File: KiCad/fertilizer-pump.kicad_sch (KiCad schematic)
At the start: 4 parts, among them U2 ESP32-S3-WROOM-1

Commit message: Save project baseline before power supply and USB changes
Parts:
- added J1: Conn_01x04, symbol Connector_Generic:Conn_01x04
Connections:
- net +3.3V: now also A1.10 (VDD), A2.10 (VDD); no longer A1.15 (GND), A2.15 (GND)
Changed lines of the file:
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@@
 		(pin "14"
 		)
-		(pin "15"
+		(pin "10"
 		)
 		(instances
@@
 	)
 	(symbol
-		(lib_name "BTT TMC2209_1")
 		(lib_id "fertilizer-pump:BTT TMC2209")
 		(at 128.27 62.23 0)
@@
 		(pin "14"
 		)
-		(pin "15"
+		(pin "10"
 		)
 		(instances
@@
 					(unit 1)
 				)
+			)
+		)
+	)
+	(symbol
+		(lib_id "Connector_Generic:Conn_01x04")
+		(at 72.39 111.76 0)
+		(unit 1)
+		(body_style 1)
+		(exclude_from_sim no)
+		(in_bom yes)
+		(on_board yes)
+		(in_pos_files yes)
+		(dnp no)
+		(fields_autoplaced yes)
+		(property "Reference" "J1"
+			(at 74.93 111.7599 0)
+			(show_name no)
+			(do_not_autoplace no)
+			(effects
+				(font
+					(size 1.27 1.27)
+				)
+				(justify left)
+			)
+		)
+		(property "Value" "Conn_01x04"
+			(at 74.93 114.2999 0)
+			(show_name no)
+			(do_not_autoplace no)
+			(effects
+				(font
+					(size 1.27 1.27)
+				)
+				(justify left)
+			)
+		)
+		(property "Footprint" ""
+			(at 72.39 111.76 0)
+			(hide yes)
+			(show_name no)
+			(do_not_autoplace no)
+			(effects
+				(font
+					(size 1.27 1.27)
+				)
+			)
+		)
+		(property "Datasheet" ""
+			(at 72.39 111.76 0)
+			(hide yes)
+			(show_name no)
+			(do_not_autoplace no)
+			(effects
+				(font
+					(size 1.27 1.27)
+				)
+			)
+		)
+		(property "Description" "Generic connector, single row, 01x04, script generated (kicad-library-utils/schlib/autogen/connector/)"
+			(at 72.39 111.76 0)
+			(hide yes)
+			(show_name no)
+			(do_not_autoplace no)
+			(effects
+				(font
+					(size 1.27 1.27)
+				)
+			)
+		)
+		(pin "1"
+		)
+		(pin "3"
+		)
+		(pin "4"
+		)
+		(pin "2"
+		)
+		(instances
+			(project "fertilizer-pump"
+				(path "/156e031f-7691-48a3-975c-ba45ae33e444"
+					(reference "J1")
+					(unit 1)
+				)

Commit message: add motor connector
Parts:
- added J2: Conn_01x04, Connector_JST:JST_XH_B4B-XH-A_1x04_P2.50mm_Vertical, symbol Connector_Generic:Conn_01x04
- added R2, R3: 10K, symbol Device:R_Small
- J1: footprint (none) -> Connector_JST:JST_XH_B4B-XH-A_1x04_P2.50mm_Vertical
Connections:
- net +3.3V: now also R2.2, R3.2
- net DRIV1.A1: now also J1.4 (Pin_4)
- net DRIV1.A2: now also J1.2 (Pin_2)
- net DRIV1.B1: now also J1.3 (Pin_3)
- net DRIV1.B2: now also J1.1 (Pin_1)
- net DRIV1.DIR: now also U2.6 (GPIO6/TOUCH6/ADC1_CH5)
- net DRIV1.STEP: now also U2.5 (GPIO5/TOUCH5/ADC1_CH4)
- net DRIV2.A1: now also J2.4 (Pin_4)
- net DRIV2.A2: now also J2.2 (Pin_2)
- net DRIV2.B1: now also J2.3 (Pin_3)
- net DRIV2.B2: now also J2.1 (Pin_1)
- net DRIV2.DIR: now also U2.17 (GPIO9/TOUCH9/ADC1_CH8/FSPIHD/SUBSPIHD)
- net DRIV2.STEP: now also U2.12 (GPIO8/TOUCH8/ADC1_CH7/SUBSPICS1)
- net DRIV.ENABLE: now reaches A1.1 (ENABLE)
- net DRIV.ENABLE: now also A2.1 (ENABLE)
- net DRIV.UART.RX_{uC}: now reaches U2.38 (GPIO2/TOUCH2/ADC1_CH1)
- net DRIV.UART.TX_{MCU}: now reaches U2.39 (GPIO1/TOUCH1/ADC1_CH0)
- net ~{DRIV1.ENABLE}: now reaches U2.4 (GPIO4/TOUCH4/ADC1_CH3)
- net ~{DRIV2.ENABLE}: now reaches U2.7 (GPIO7/TOUCH7/ADC1_CH6)
- new net DRIV1.ENABLE: R3.1
- new net DRIV2.ENABLE: R2.1
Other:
- moved on the sheet: J1

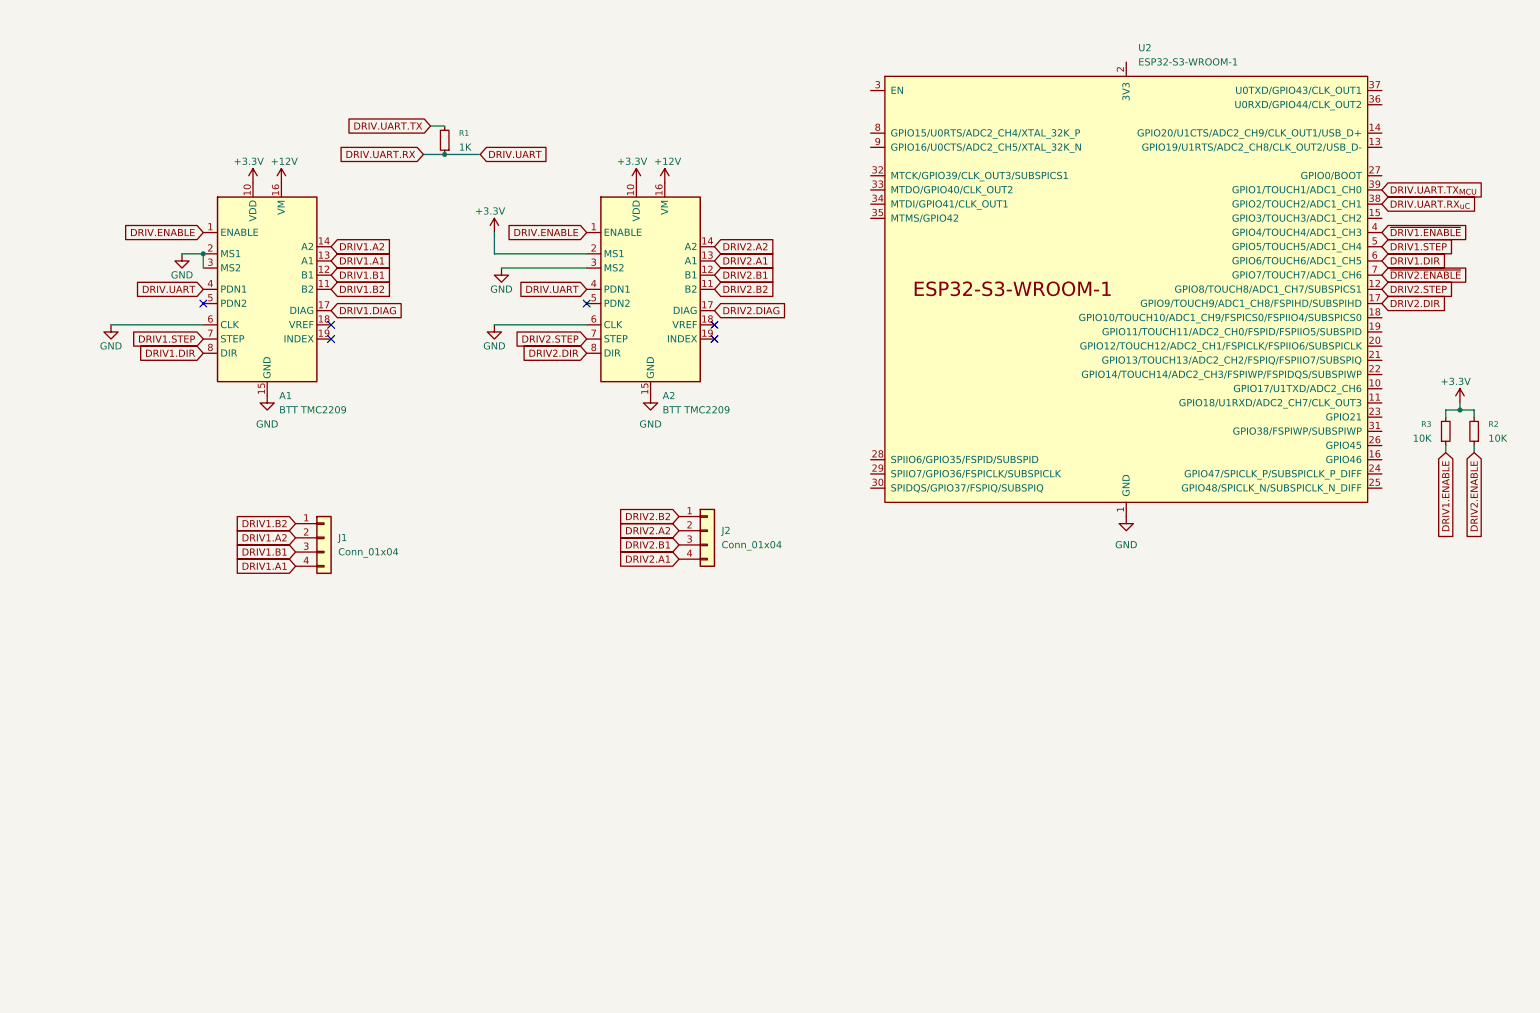
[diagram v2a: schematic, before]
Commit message: add pd trigger board, usb-c
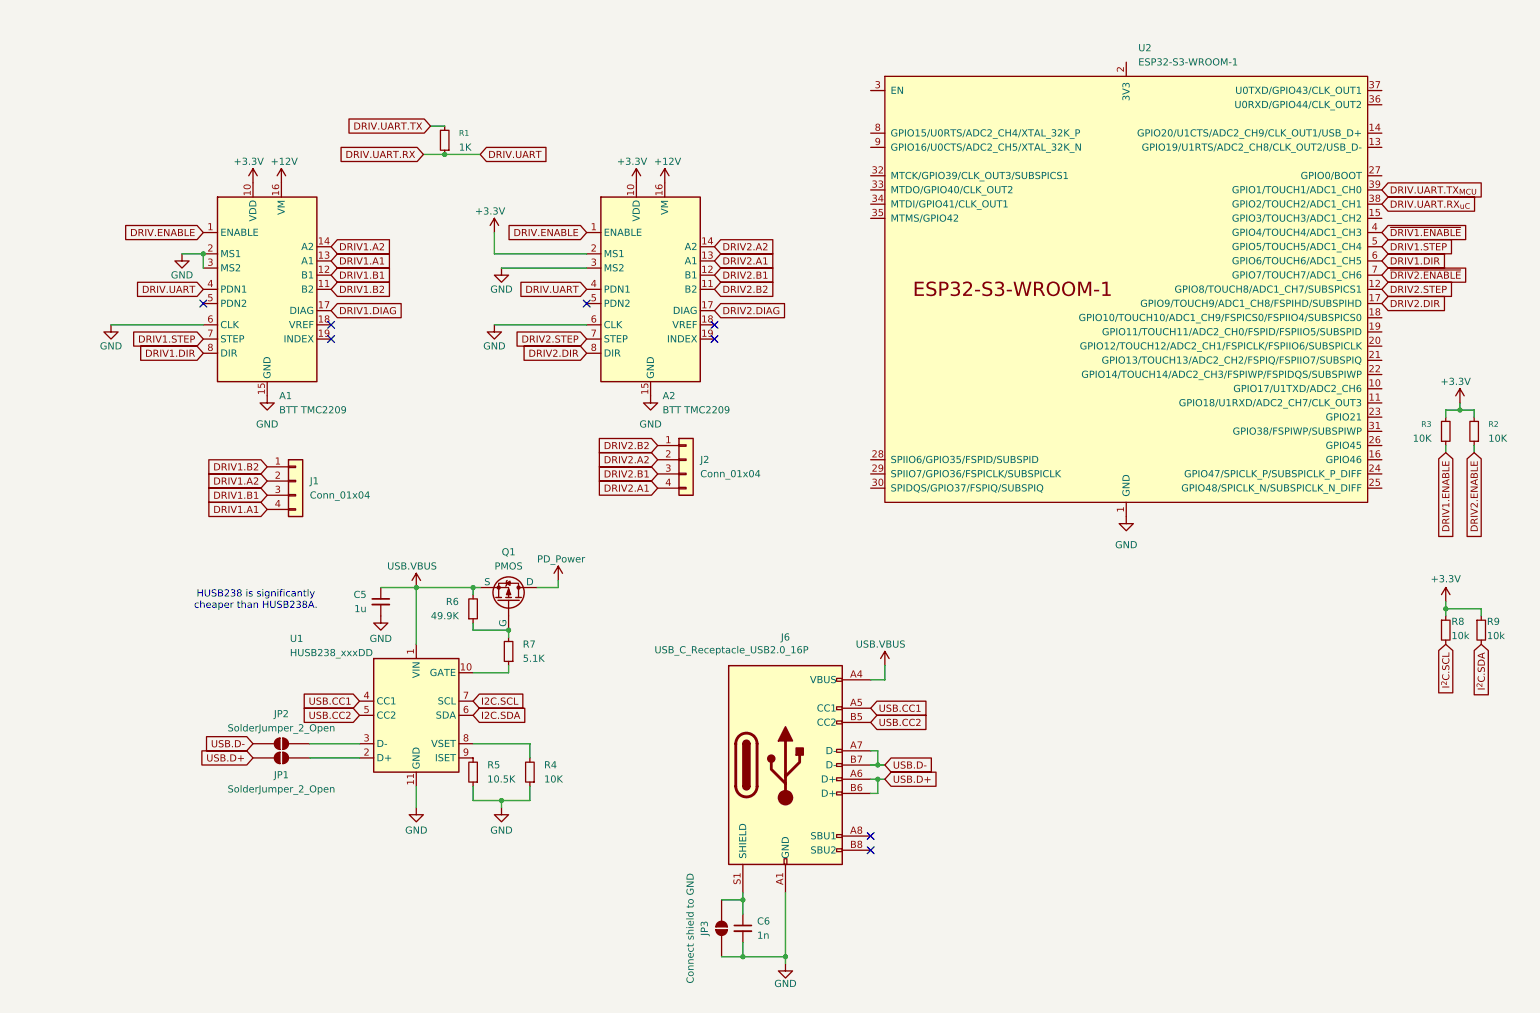
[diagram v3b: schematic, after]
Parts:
- added C5: 1u, Capacitor_SMD:C_0805_2012Metric_Pad1.18x1.45mm_HandSolder, symbol Device:C_Small
- added C6: 1n, Capacitor_SMD:C_0805_2012Metric_Pad1.18x1.45mm_HandSolder, symbol Device:C_Small
- added J6: USB_C_Receptacle_USB2.0_16P, Connector_USB:USB_C_Receptacle_GCT_USB4105-xx-A_16P_TopMnt_Horizontal, symbol Connector:USB_C_Receptacle_USB2.0_16P
- added JP1, JP2: SolderJumper_2_Open, symbol Jumper:SolderJumper_2_Open
- added JP3: Connect shield to GND, symbol Jumper:SolderJumper_2_Open
- added Q1: PMOS, symbol Simulation_SPICE:PMOS
- added R4: 10K, symbol Device:R_Small
- added R5: 10.5K, symbol Device:R_Small
- added R6: 49.9K, symbol Device:R_Small
- added R7: 5.1K, symbol Device:R_Small
- added R8, R9: 10k, Resistor_SMD:R_0805_2012Metric_Pad1.20x1.40mm_HandSolder, symbol Device:R_Small
- added U1: HUSB238_xxxDD, Package_DFN_QFN:WDFN-10-1EP_3x3mm_P0.5mm_EP1.8x2.5mm_ThermalVias, symbol Interface_USB:HUSB238_xxxDD
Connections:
- net +3.3V: now also R8.1, R9.1
- net GND: now also C5.2, C6.2, J6.A1 (GND), J6.A12 (GND), J6.B1 (GND), J6.B12 (GND), JP3.1 (A), R4.1, R5.1, U1.11 (GND)
- new net: Q1.2 (G), R6.1, R7.2
- new net: JP1.2 (B), U1.2 (D+)
- new net: C6.1, J6.S1 (SHIELD), JP3.2 (B)
- new net: R4.2, U1.8 (VSET)
- new net: R5.2, U1.9 (ISET)
- new net: JP2.2 (B), U1.3 (D-)
- new net: R7.1, U1.10 (GATE)
- new net I2C.SCL: U1.7 (SCL)
- new net I2C.SDA: U1.6 (SDA)
- new net I^{2}C.SCL: R8.2
- new net I^{2}C.SDA: R9.2
- new net PD_Power: Q1.1 (D)
- new net USB.CC1: J6.A5 (CC1), U1.4 (CC1)
- new net USB.CC2: J6.B5 (CC2), U1.5 (CC2)
- new net USB.D+: J6.A6 (D+), J6.B6 (D+), JP1.1 (A)
- new net USB.D-: J6.A7 (D-), J6.B7 (D-), JP2.1 (A)
- new net USB.VBUS: C5.1, J6.A4 (VBUS), J6.A9 (VBUS), J6.B4 (VBUS), J6.B9 (VBUS), Q1.3 (S), R6.2, U1.1 (VIN)
- no-connect marks 6 -> 8
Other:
- note added: "HUSB238 is significantly cheaper than HUSB238A."
- moved on the sheet: J1, J2

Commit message: .
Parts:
- added D1, D2: ESD762, Package_TO_SOT_SMD:SOT-23_Handsoldering, symbol Device:D_TVS_Dual_AAC
- added D3: D_Zener, Diode_SMD:D_SOD-123F, symbol Device:D_Zener
- A1, A2: footprint Module:Pololu_Breakout-16_15.2x20.3mm -> fertilizer-pump:BTT TMC2209
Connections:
- net GND: now also D1.3 (common), D2.3 (common), D3.2 (A)
- net USB.CC1: now also D2.1 (A1)
- net USB.CC2: now also D2.2 (A2)
- net USB.D+: now also D1.1 (A1)
- net USB.D-: now also D1.2 (A2)
- net USB.VBUS: now also D3.1 (K)
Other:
- note added: "ESD Protection"
- note added: "FIX: wrong footprint SOD123FL instead of SOD123F"
- moved on the sheet: C5, JP1, JP2, Q1, R4, R5, R6, R7, U1

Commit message: refactor,
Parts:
- removed A1, A2: BTT TMC2209, fertilizer-pump:BTT TMC2209, symbol fertilizer-pump:BTT TMC2209
- removed C5: 1u, Capacitor_SMD:C_0805_2012Metric_Pad1.18x1.45mm_HandSolder, symbol Device:C_Small
- removed C6: 1n, Capacitor_SMD:C_0805_2012Metric_Pad1.18x1.45mm_HandSolder, symbol Device:C_Small
- removed D1, D2: ESD762, Package_TO_SOT_SMD:SOT-23_Handsoldering, symbol Device:D_TVS_Dual_AAC
- removed D3: D_Zener, Diode_SMD:D_SOD-123F, symbol Device:D_Zener
- removed J1, J2: Conn_01x04, Connector_JST:JST_XH_B4B-XH-A_1x04_P2.50mm_Vertical, symbol Connector_Generic:Conn_01x04
- removed J6: USB_C_Receptacle_USB2.0_16P, Connector_USB:USB_C_Receptacle_GCT_USB4105-xx-A_16P_TopMnt_Horizontal, symbol Connector:USB_C_Receptacle_USB2.0_16P
- removed JP1, JP2: SolderJumper_2_Open, symbol Jumper:SolderJumper_2_Open
- removed JP3: Connect shield to GND, symbol Jumper:SolderJumper_2_Open
- removed Q1: PMOS, symbol Simulation_SPICE:PMOS
- removed R1: 1K, symbol Device:R_Small
- removed R4: 10K, symbol Device:R_Small
- removed R5: 10.5K, symbol Device:R_Small
- removed R6: 49.9K, symbol Device:R_Small
- removed R7: 5.1K, symbol Device:R_Small
- removed U1: HUSB238_xxxDD, Package_DFN_QFN:WDFN-10-1EP_3x3mm_P0.5mm_EP1.8x2.5mm_ThermalVias, symbol Interface_USB:HUSB238_xxxDD
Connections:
- no-connect marks 8 -> 0
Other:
- added sheet Power (power.kicad_sch)
- added sheet Stepper (stepper.kicad_sch)
- note removed: "ESD Protection"
- note removed: "FIX: wrong footprint SOD123FL instead of SOD123F"
- note removed: "HUSB238 is significantly cheaper than HUSB238A."

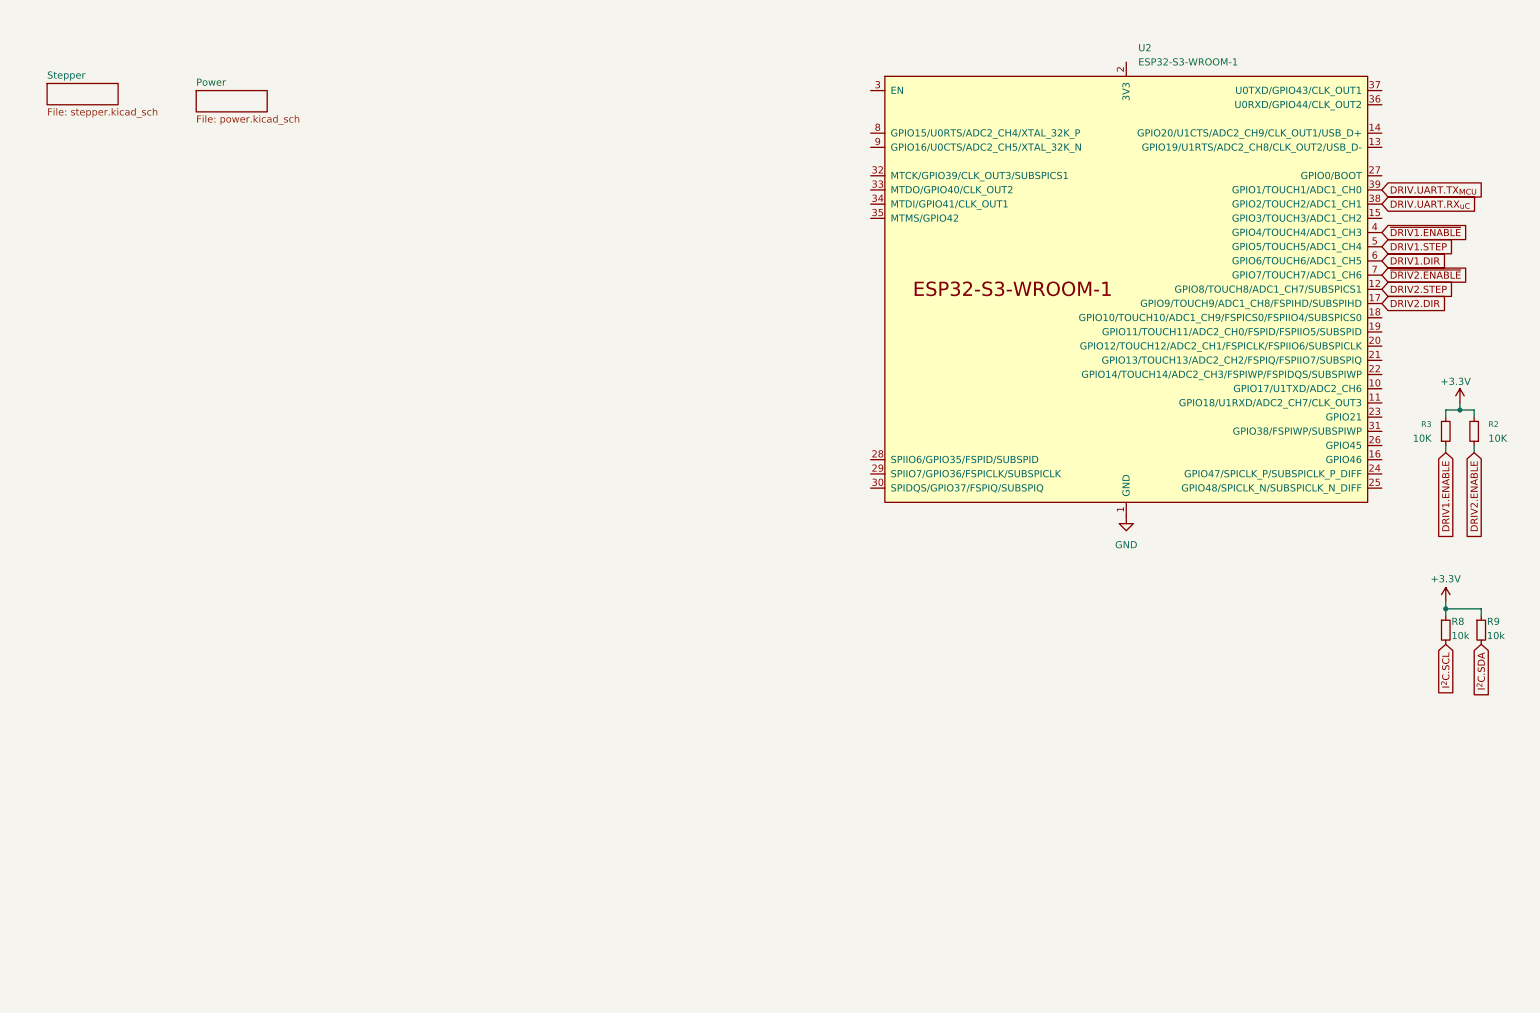
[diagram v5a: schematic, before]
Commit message: add buck converter, fix footprints
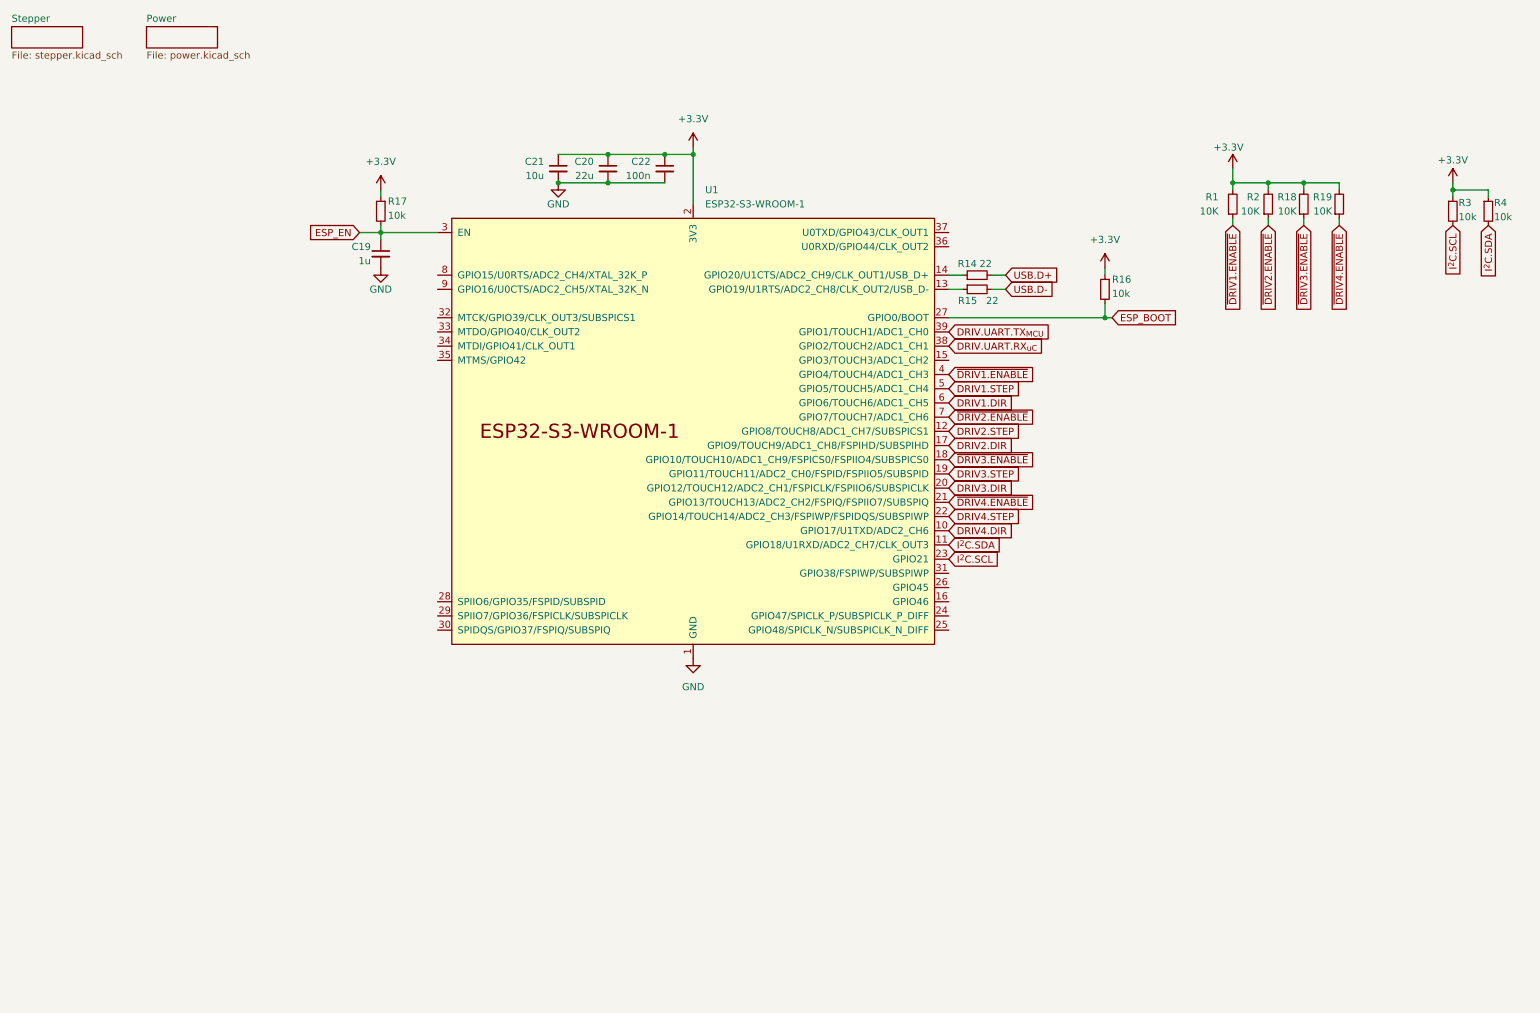
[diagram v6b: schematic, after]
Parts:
- added C19: 1u, Capacitor_SMD:C_0805_2012Metric_Pad1.18x1.45mm_HandSolder, symbol Device:C_Small
- added C20: 22u, Capacitor_SMD:C_0805_2012Metric_Pad1.18x1.45mm_HandSolder, symbol Device:C_Small
- added C21: 10u, Capacitor_SMD:C_0805_2012Metric_Pad1.18x1.45mm_HandSolder, symbol Device:C_Small
- added C22: 100n, Capacitor_SMD:C_0805_2012Metric_Pad1.18x1.45mm_HandSolder, symbol Device:C_Small
- added R14, R15: 22, Resistor_SMD:R_0805_2012Metric_Pad1.20x1.40mm_HandSolder, symbol Device:R_Small
- added R16, R17: 10k, Resistor_SMD:R_0805_2012Metric_Pad1.20x1.40mm_HandSolder, symbol Device:R_Small
- added R18, R19: 10K, symbol Device:R_Small
- renumbered R3 to R1, R8 to R3, R9 to R4, U2 to U1
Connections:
- net DRIV1.ENABLE is gone; now on net ~{DRIV1.ENABLE}: R1.1
- net DRIV2.ENABLE is gone; now on net ~{DRIV2.ENABLE}: R2.1
- net +3.3V: now also U1.2 (3V3), C20.1, C21.1, C22.1, R16.1, R17.1, R18.2, R19.2
- net GND: now also C19.2, C20.2, C21.2, C22.2
- net I^{2}C.SCL: now also U1.23 (GPIO21)
- net I^{2}C.SDA: now also U1.11 (GPIO18/U1RXD/ADC2_CH7/CLK_OUT3)
- net DRIV4.DIR: now reaches U1.10 (GPIO17/U1TXD/ADC2_CH6)
- net at U1.13 (GPIO19/U1RTS/ADC2_CH8/CLK_OUT2/USB_D-): now also R15.1
- net at U1.14 (GPIO20/U1CTS/ADC2_CH9/CLK_OUT1/USB_D+): now also R14.1
- net ~{DRIV3.ENABLE}: now reaches U1.18 (GPIO10/TOUCH10/ADC1_CH9/FSPICS0/FSPIIO4/SUBSPICS0)
- net ~{DRIV3.ENABLE}: now also R18.1
- net DRIV3.STEP: now reaches U1.19 (GPIO11/TOUCH11/ADC2_CH0/FSPID/FSPIIO5/SUBSPID)
- net DRIV3.DIR: now reaches U1.20 (GPIO12/TOUCH12/ADC2_CH1/FSPICLK/FSPIIO6/SUBSPICLK)
- net ~{DRIV4.ENABLE}: now reaches U1.21 (GPIO13/TOUCH13/ADC2_CH2/FSPIQ/FSPIIO7/SUBSPIQ)
- net ~{DRIV4.ENABLE}: now also R19.1
- net DRIV4.STEP: now reaches U1.22 (GPIO14/TOUCH14/ADC2_CH3/FSPIWP/FSPIDQS/SUBSPIWP)
- net ESP_BOOT: now reaches U1.27 (GPIO0/BOOT)
- net ESP_BOOT: now also R16.2
- net ESP_EN: now reaches U1.3 (EN)
- net ESP_EN: now also C19.1, R17.2
- new net USB.D+: R14.2
- new net USB.D-: R15.2
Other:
- moved on the sheet: R1, R3, R4, U1
